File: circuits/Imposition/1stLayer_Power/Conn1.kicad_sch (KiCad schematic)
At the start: 12 parts, among them J11 Conn_01x02_Male, J8 Conn_01x08_MountingPin

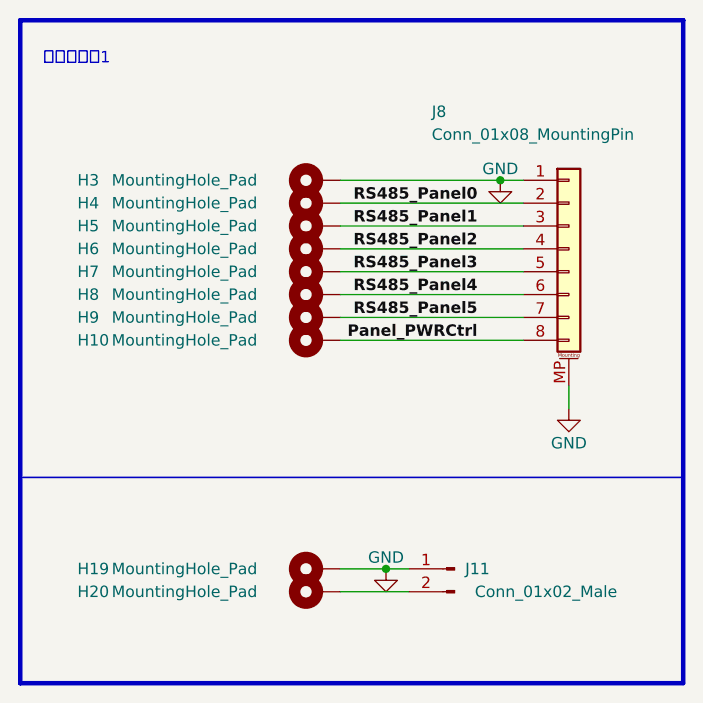
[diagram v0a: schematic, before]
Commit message: 発注_第一弾
Drive, 1stLayer_Power, 2ndLayer_3rdLayer
を発注
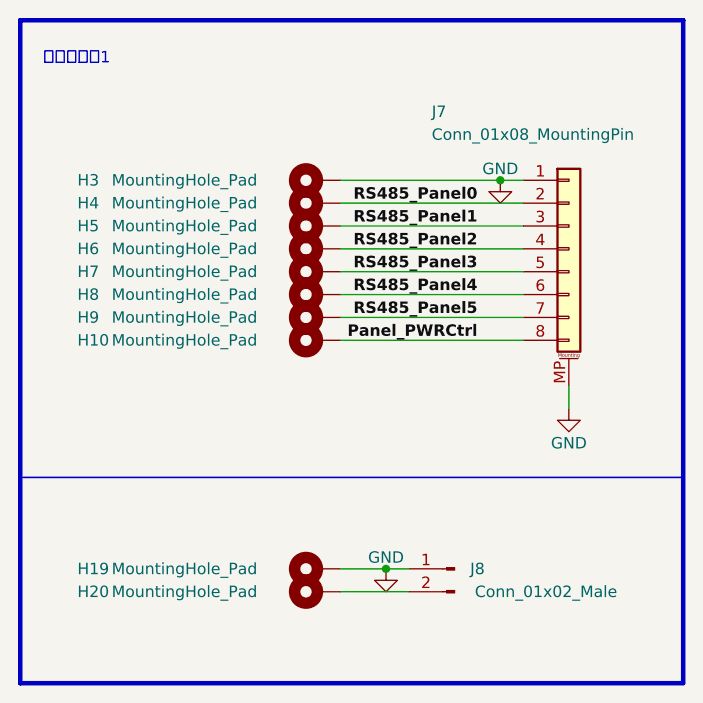
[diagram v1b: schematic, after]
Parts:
- renumbered J8 to J7, J11 to J8
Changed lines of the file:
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@@
   (symbol (lib_id "Connector:Conn_01x02_Male") (at 157.48 129.54 0) (mirror y) (unit 1)
     (in_bom yes) (on_board yes) (dnp no)
-    (property "Reference" "J11" (at 160.02 129.54 0)
+    (property "Reference" "J8" (at 160.02 129.54 0)
       (effects (font (size 1.27 1.27)))
     )
@@
       (project "1stLayer_Power"
         (path "/599e2e4a-5379-461e-b684-22a177410a52/2db03a8a-8549-43cf-b021-74f0851aa008"
-          (reference "J11") (unit 1)
+          (reference "J8") (unit 1)
         )
       )
@@
   (symbol (lib_id "Connector_Generic_MountingPin:Conn_01x08_MountingPin") (at 170.18 93.98 0) (unit 1)
     (in_bom yes) (on_board yes) (dnp no)
-    (property "Reference" "J8" (at 154.94 78.74 0)
+    (property "Reference" "J7" (at 154.94 78.74 0)
       (effects (font (size 1.27 1.27)) (justify left))
     )
@@
       (project "1stLayer_Power"
         (path "/599e2e4a-5379-461e-b684-22a177410a52/2db03a8a-8549-43cf-b021-74f0851aa008"
-          (reference "J8") (unit 1)
-        )
-      )
+          (reference "J7") (unit 1)
+        )
+      )
